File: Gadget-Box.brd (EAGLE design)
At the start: 96 x 56 mm, 41 parts, among them SW1 OS102011MA1Q, U1 MCP73831T-2ACI/OT, U2 AP2112-3.3, U3 ATMEGA32U4-XUMU, U4 ATMEGA32U4-XUAU, X1 JSTPH, Y1 16MHz KX-7

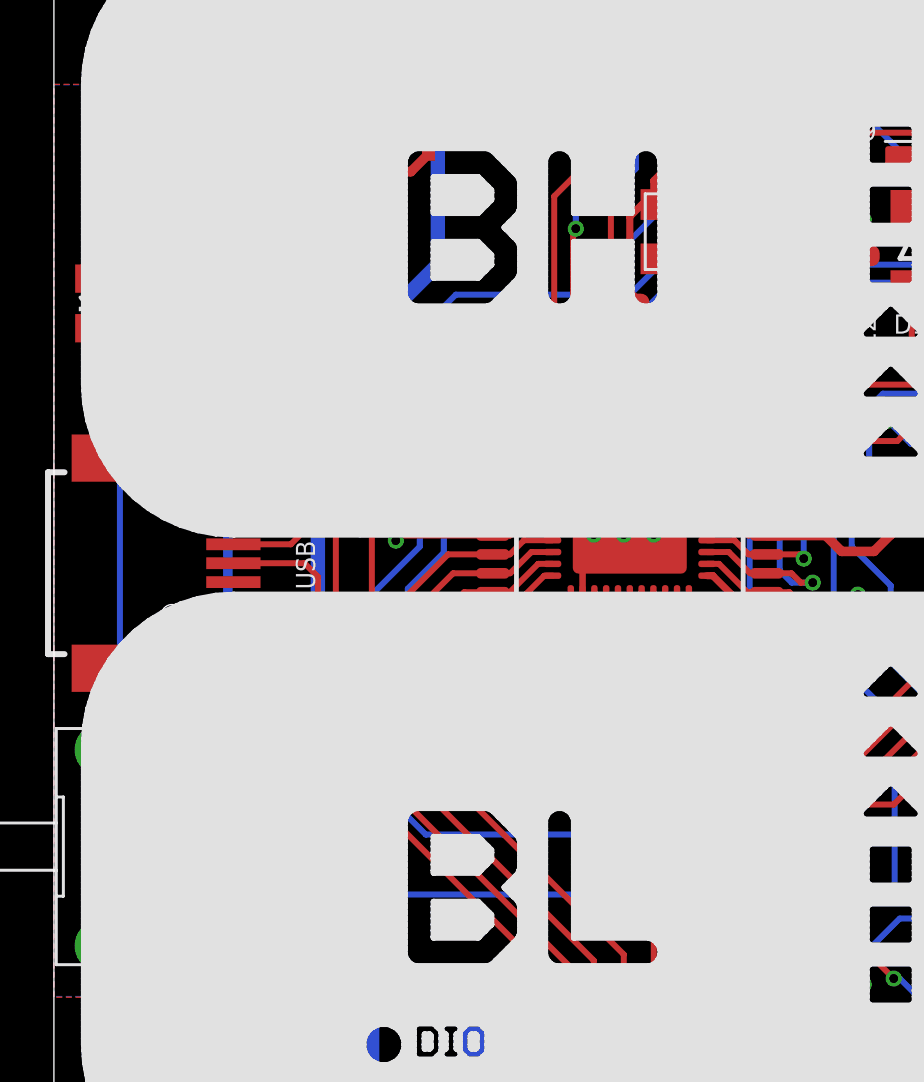
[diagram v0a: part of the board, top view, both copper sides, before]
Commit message: Version 1.6 - Changed Crystal to 8Mhz and 16Mhz footprint.
Updated silkscreen
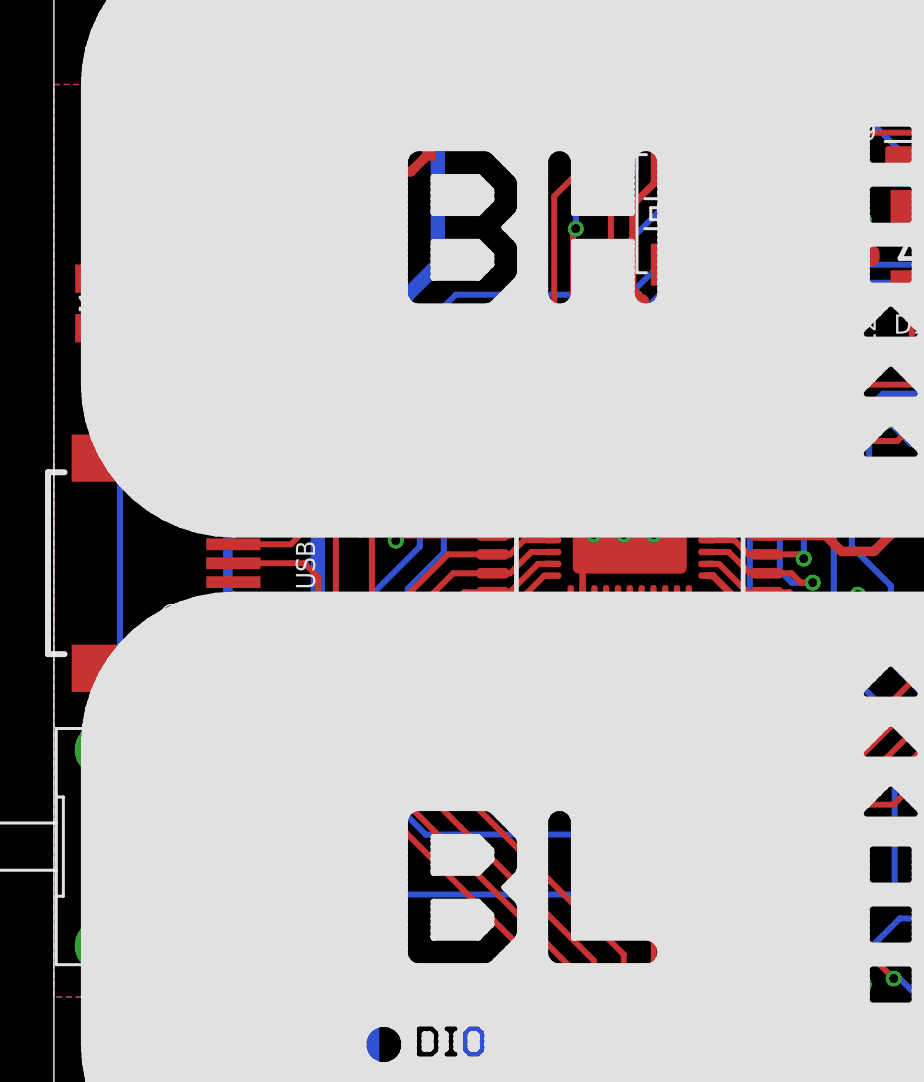
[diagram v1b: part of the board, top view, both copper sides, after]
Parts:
- removed Y1: 16MHz KX-7, SmartPrj:CRYSTAL-3.2-2.5
- added X2: CRYSTAL-0500290P1, OPL Eagle Library:2P-SMD-5.0X3.2
- C1, C8: value 100n -> .1uF
- R5: value 10K\ -> 10K
- moved U$12 15.1 mm to (83.6, 28.7), turned to 270 degrees
- moved U$13 12.9 mm to (25.7, 28.7), turned to 270 degrees
- renumbered SW1 to PSW1
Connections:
- net GND: no longer Y1.2, Y1.4
- net XTAL1: now also X2.1; no longer Y1.1
- net XTAL2: now also X2.2; no longer Y1.3
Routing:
- net GND: track 81.8 -> 74.4 mm, vias 20 -> 19
- net XTAL2: track 10.4 -> 11.0 mm
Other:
- board text added: "Gadget Box Copyright 2016 Gadget Factory, LLC Version 1.6"
- board text removed: "Gadget Box Copyright 2016 Gadget Factory, LLC Version 1.5.1"

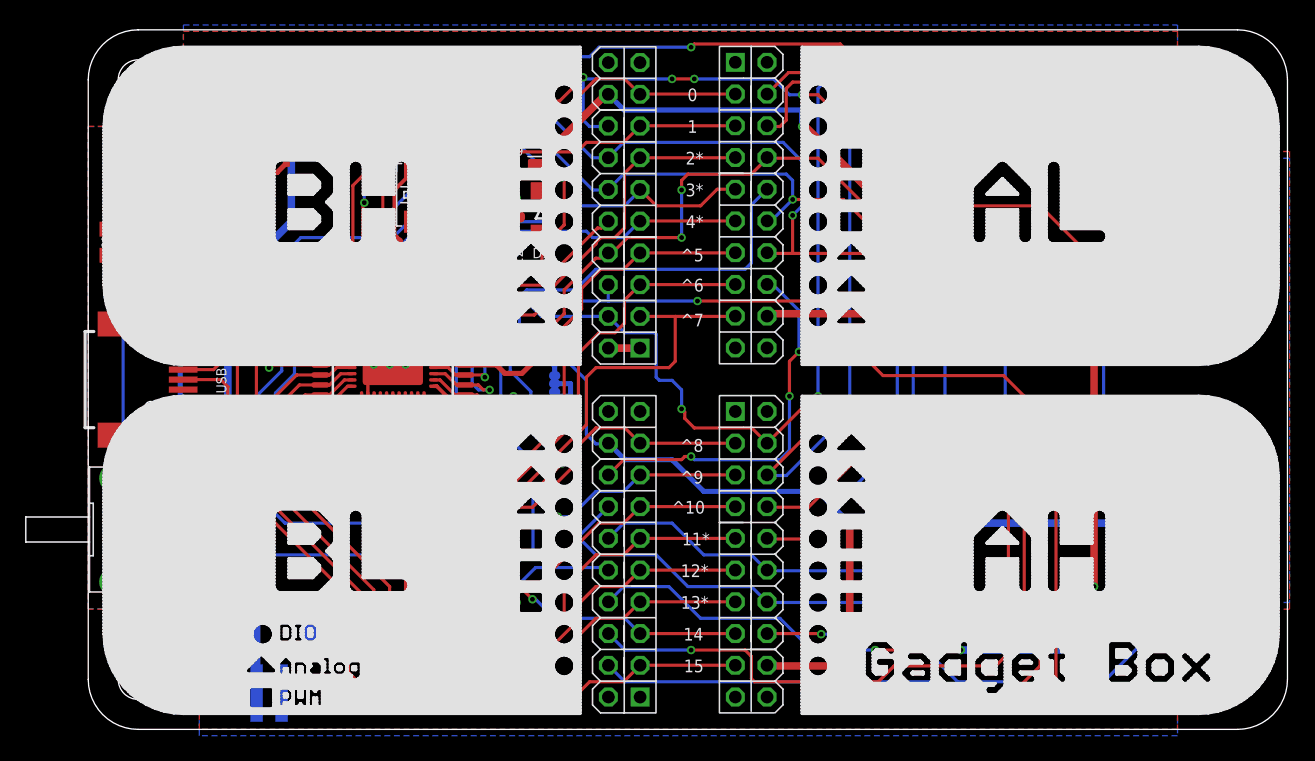
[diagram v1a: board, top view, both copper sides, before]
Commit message: GadgetBox - Version 1.7
7/6/2016 V1.6 GadgetBox
Changed size of board to fit white cases. 93.5x53.5
Added voltage divider to allow capturing battery power on pin D5.
Added all BOM info.
Rerouted 3.3v and GND to provide better paths.
Moved location of compontents for the BH silkscreen and the new board
size.
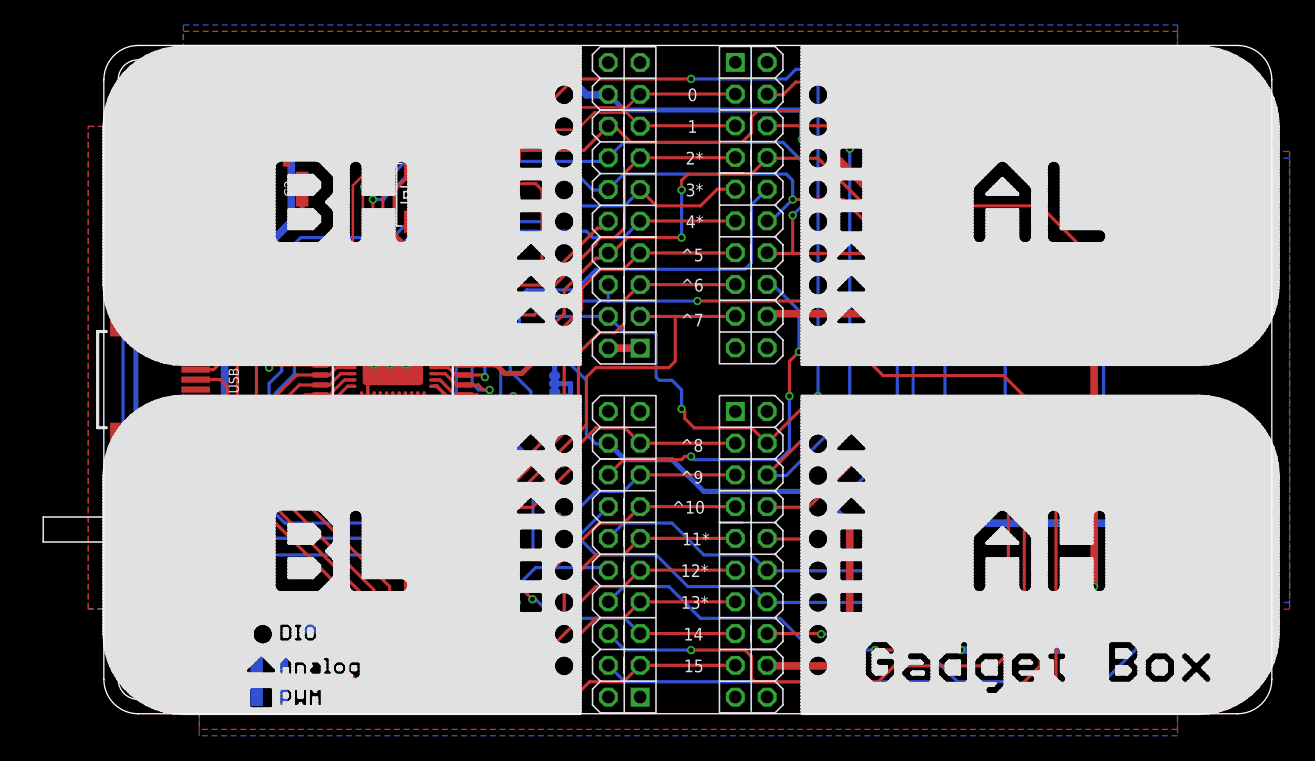
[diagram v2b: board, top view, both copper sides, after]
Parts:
- removed U$6: (no value), eCogs:ECOG9656_V1
- added R10: DNP, GadgetFactory:0603
- added R11, R12: 100k, GadgetFactory:0603
- added U$8: (no value), eCogs:ECOG93P53P5
- moved D1 6.41 mm to (32.3, 46.4), turned to 0 degrees
- moved C2 4.18 mm to (17.1, 43.3), turned to 270 degrees
- moved R9 2.74 mm to (32.3, 43.9)
- moved C6 2.03 mm to (4.15, 45.1)
- moved PSW1 1.40 mm to (3.40, 16.0)
- moved C9 1.37 mm to (29.5, 43.7)
- moved X1 1.27 mm to (14.5, 7.87)
- moved CHG 1.20 mm to (2.70, 39.0)
- moved USB 1.00 mm to (6.00, 28.0)
- moved C12 0.64 mm to (33.8, 40.1)
- moved L1 0.51 mm to (32.1, 40.1)
- moved C8 0.38 mm to (30.4, 40.1)
- moved R5 0.36 mm to (12.3, 36.6)
- moved C10 0.25 mm to (32.5, 23.2)
- moved C7 0.25 mm to (28.6, 40.1)
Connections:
- removed net +3V3: C2.1, C3.1, U2.5
- new net N$2: R10.2, R11.1, R12.2
- net 3V3: now also C2.1, C3.1, U2.5
- net D5/A5: now also R10.1
- net GND: now also R12.1
- net VBAT: now also R11.2
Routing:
- net D5/A5: track 44.2 -> 74.5 mm, vias 0 -> 4
- net 3V3: track 98.1 -> 84.9 mm, vias 13 -> 14
- net RESET: track 234.6 -> 222.5 mm, vias 12 -> 6
- net I2C-SDA: track 124.2 -> 113.3 mm
- net I2C-SCL: track 138.3 -> 128.3 mm
- net +3V3: track 9.73 -> 0.00 mm, vias 1 -> 0
- net SPI-MOSI: track 152.5 -> 146.3 mm
- net SPI-CS4: track 109.9 -> 105.9 mm
- net N$2: track 0.00 -> 3.39 mm
- net N$3: track 13.1 -> 16.5 mm
- net SPI-MISO: track 146.4 -> 143.5 mm
- net VBUS: track 279.5 -> 281.8 mm, vias 11 -> 7
- net GND: track 74.4 -> 72.9 mm, vias 19 -> 20
- net XTAL1: track 17.5 -> 16.0 mm
- net D0/RX: track 47.7 -> 46.7 mm
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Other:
- board size 96 x 56 mm -> 93.5 x 53.5 mm
- board text added: "Gadget Box Copyright 2016 Gadget Factory, LLC Version 1.7"
- board text removed: "Gadget Box Copyright 2016 Gadget Factory, LLC Version 1.6"

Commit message: GadgetBox V1.7
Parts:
- removed C12: 1uF, SmartPrj:C0603-ROUND
- removed D4: MBR120, microbuilder:SOD-123
- removed X2: CRYSTAL-0500290P1, OPL Eagle Library:2P-SMD-5.0X3.2
- added C5: .1uF, SmartPrj:C0603-ROUND
- added D2: CD1206-S01575, diode:MINIMELF
- added X100: JSTPH, microbuilder:JSTPH2
- C1: value .1uF -> 10µF; device SmartPrj:C0603-ROUND -> microbuilder:0805-NO
- C10: value .1uF -> 1uF; device SmartPrj:C0603-ROUND -> GadgetFactory:0603
- C11: device SmartPrj:C0603-ROUND -> GadgetFactory:0603
- C2: value 1uF -> 10µF; device microbuilder:0603-NO -> microbuilder:0805-NO
- C4: value 10µF -> 1uF; device microbuilder:0805-NO -> GadgetFactory:0603
- C6: value 10µF -> 22p; device microbuilder:0805-NO -> SmartPrj:C0603-ROUND
- C9: value 22p -> .1uF
- D1: value CD1206-S01575 -> MBR120; device diode:MINIMELF -> microbuilder:SOD-123
- R1: value 22R -> 1K; device GadgetFactory_6.0:0805 -> microbuilder:0603-NO
- R10: value DNP -> 10K; device GadgetFactory:0603 -> GadgetFactory_6.0:0603
- R11, R12: value 100k -> 10K
- R2: value 1K -> 100k; device microbuilder:0603-NO -> GadgetFactory:0603
- R3: value 10K -> DNP; device GadgetFactory_6.0:0805 -> GadgetFactory:0603
- R5: value 10K -> 100k; device microbuilder:0603-NO -> GadgetFactory:0603
- R6: device SmartPrj:R0805 -> GadgetFactory:0603
- R7: value 10K -> 22R; device SmartPrj:R0805 -> GadgetFactory_6.0:0805
- R8: value 1M -> 10K; device SmartPrj:R0603-ROUND -> GadgetFactory_6.0:0603
- R9: value 10K -> 1M; device GadgetFactory_6.0:0805 -> SmartPrj:R0603-ROUND
- U3: value ATMEGA32U4-XUMU -> ATMEGA32U4-XUAU; device SmartPrj:QFN44ML7X7 -> SmartPrj:TQFP44-PAD
- U4: value ATMEGA32U4-XUAU -> ATMEGA32U4-XUMU; device SmartPrj:TQFP44-PAD -> SmartPrj:QFN44ML7X7
- X1: value JSTPH -> CRYSTAL-0500290P1; device microbuilder:JSTPH2 -> OPL Eagle Library:2P-SMD-5.0X3.2
- moved R12 66.1 mm to (71.1, 32.5)
- moved R11 61.8 mm to (68.3, 35.6), turned to 90 degrees
- moved R6 58.9 mm to (12.3, 36.6), turned to 180 degrees
- moved R7 54.1 mm to (14.2, 34.0), turned to 0 degrees
- moved X1 36.9 mm to (26.3, 42.8), flipped to the top, turned to 270 degrees
- moved R10 36.3 mm to (32.3, 43.9), turned to 180 degrees
- moved C1 29.2 mm to (4.15, 45.1), turned to 90 degrees
- moved C6 24.9 mm to (28.6, 40.1)
- moved R2 23.6 mm to (8.00, 13.0), turned to 90 degrees
- moved R5 21.7 mm to (10.0, 15.0), turned to 0 degrees
- moved C9 20.7 mm to (32.5, 23.2)
- moved R8 18.9 mm to (17.5, 21.8), turned to 90 degrees
- moved C10 16.9 mm to (33.8, 40.1), turned to 90 degrees
- moved D1 16.8 mm to (16.3, 51.6), turned to 180 degrees
- moved R1 16.4 mm to (4.57, 36.3)
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- renumbered U$12 to U$101, U$13 to U$100, U$8 to $$U$1
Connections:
- net 3V3: now also C4.2, C5.1, D2.C, R10.2, R11.2, R12.2; no longer C1.1, C2.1, D1.C, R6.2, R7.2, R9.2
- net AGND: now also C9.1; no longer C10.1
- net AREF: now also C9.2; no longer C10.2
- net AVCC: now also C10.1; no longer C12.1
- net D+: now also R4.1; no longer R1.1
- net D-: now also R7.1; no longer R4.1
- net D5/A5: now also R3.1; no longer R10.1
- net GND: now also C10.2, C4.1, C5.2, C6.1, C7.2, PSW1.3, R2.1, R6.2, R8.1, U3.P$1, U4.EXP, X100.1; no longer C12.2, C4.2, C6.2, C7.1, C9.2, PSW1.1, R12.1, R3.1, R5.2, U3.EXP, U4.P$1, X1.1
- net HWB: now also R8.2; no longer R3.2
- net I2C-SCL: now also R12.1; no longer R6.1
- net I2C-SDA: now also R11.1; no longer R7.1
- net N$1: now also R1.1; no longer R2.1
- net N$2: now also R2.2, R3.2, R5.1; no longer R10.2, R11.1, R12.2
- net N$3: now also R1.2; no longer R2.2
- net N$4: now also R6.1; no longer R5.1
- net RD+: now also R4.2; no longer R1.2
- net RD-: now also R7.2; no longer R4.2
- net RESET: now also D2.A, R10.1; no longer D1.A, R9.1
- net VBAT: now also C2.1, D1.A, R5.2, X100.2; no longer C4.1, D4.A, R11.2, X1.2
- net VBUS: now also C1.1, D1.C, PSW1.1; no longer C6.1, D4.C, PSW1.3
- net XTAL1: now also C7.1, R9.1, X1.1; no longer C9.1, R8.1, X2.1
- net XTAL2: now also C6.2, R9.2, X1.2; no longer C7.2, R8.2, X2.2
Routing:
- net GND: track 72.9 -> 75.5 mm, vias 20 -> 19
- net VBUS: track 281.8 -> 281.0 mm, vias 7 -> 8
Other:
- board text added: "Off"
- board text added: "On"
- board text removed: "CHG"
- board text removed: "D:/Dropbox/GadgetFactory_Engineering/Firefly-Box/AH.bmp"
- board text removed: "D:/Dropbox/GadgetFactory_Engineering/Firefly-Box/AL.bmp"
- board text removed: "D:/Dropbox/GadgetFactory_Engineering/Firefly-Box/BH.bmp"
- board text removed: "D:/Dropbox/GadgetFactory_Engineering/Firefly-Box/BL.bmp"
- board text removed: "D:/Dropbox/GadgetFactory_Engineering/Firefly-Box/Bus Text.bmp"
- board text removed: "D:/Dropbox/GadgetFactory_Engineering/Firefly-Box/DuinoBox.bmp"
- board text removed: "D:/Dropbox/GadgetFactory_Engineering/Firefly-Box/I2C.bmp"
- board text removed: "D:/Dropbox/GadgetFactory_Engineering/Firefly-Box/SPI.bmp"
- board text removed: "ON"

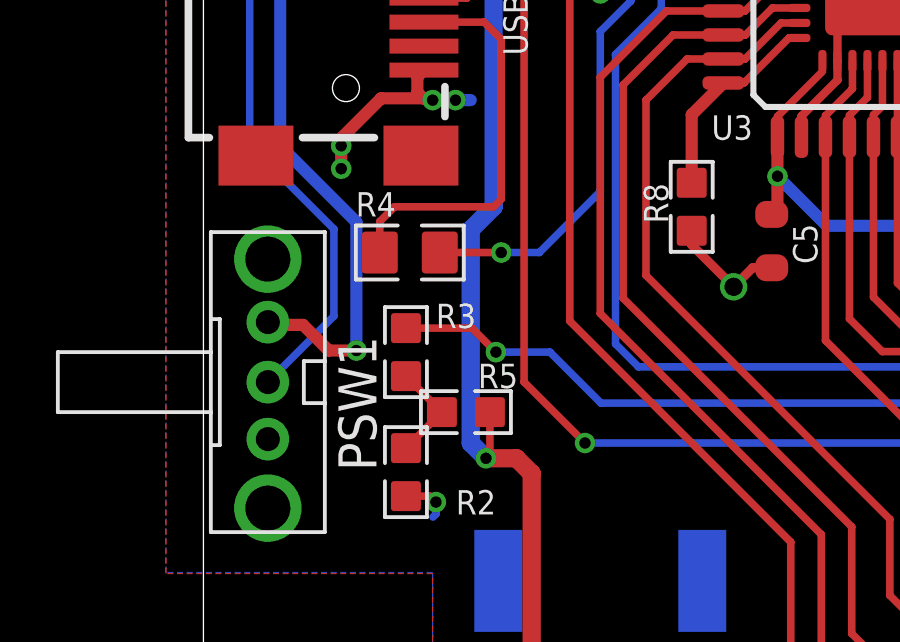
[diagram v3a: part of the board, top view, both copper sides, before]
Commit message: GadgetBox V1.7
Move the On/Off locations
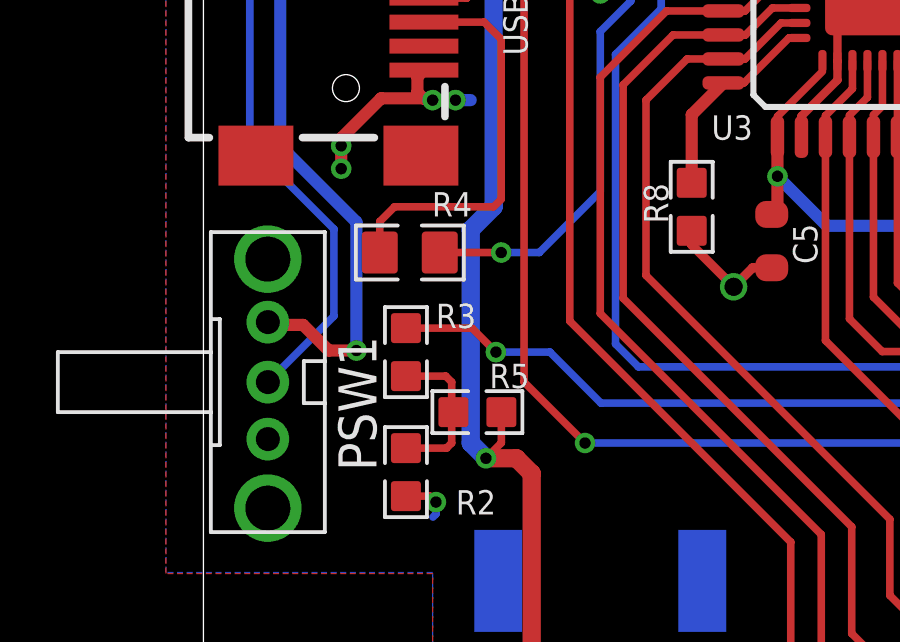
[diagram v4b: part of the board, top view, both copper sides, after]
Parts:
- moved R5 0.38 mm to (10.4, 15.0)
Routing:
- net N$2: track 3.39 -> 5.28 mm
